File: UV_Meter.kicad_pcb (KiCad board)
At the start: 2 copper layers, 58.4 x 17.8 mm, 8 parts, among them SW1 SW_Push, U1 ATtiny85-20PU

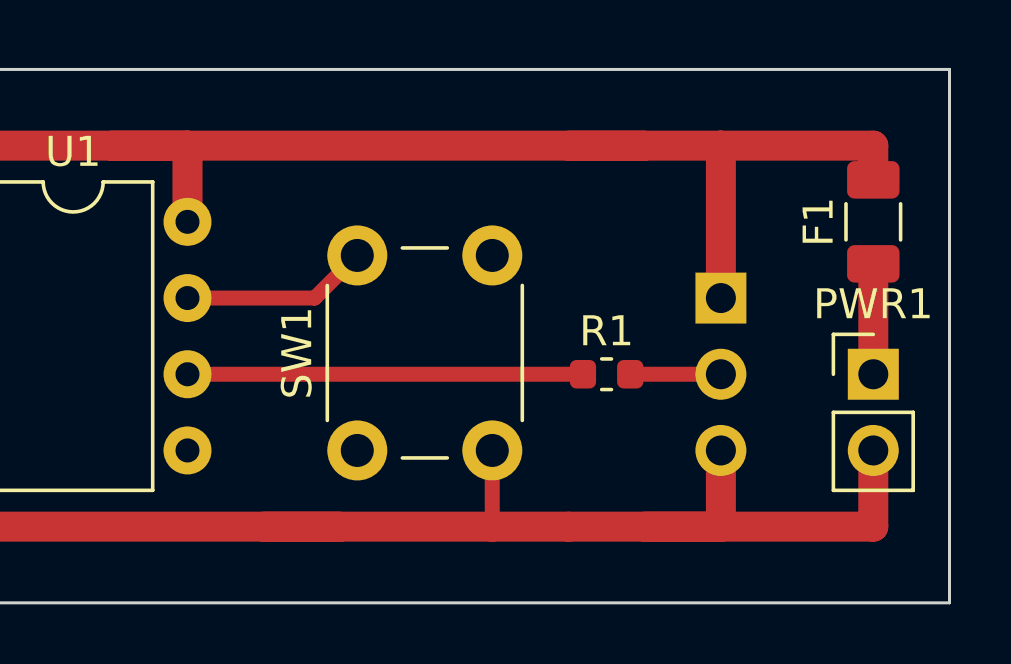
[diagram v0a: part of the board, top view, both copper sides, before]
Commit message: switched PWR & LED
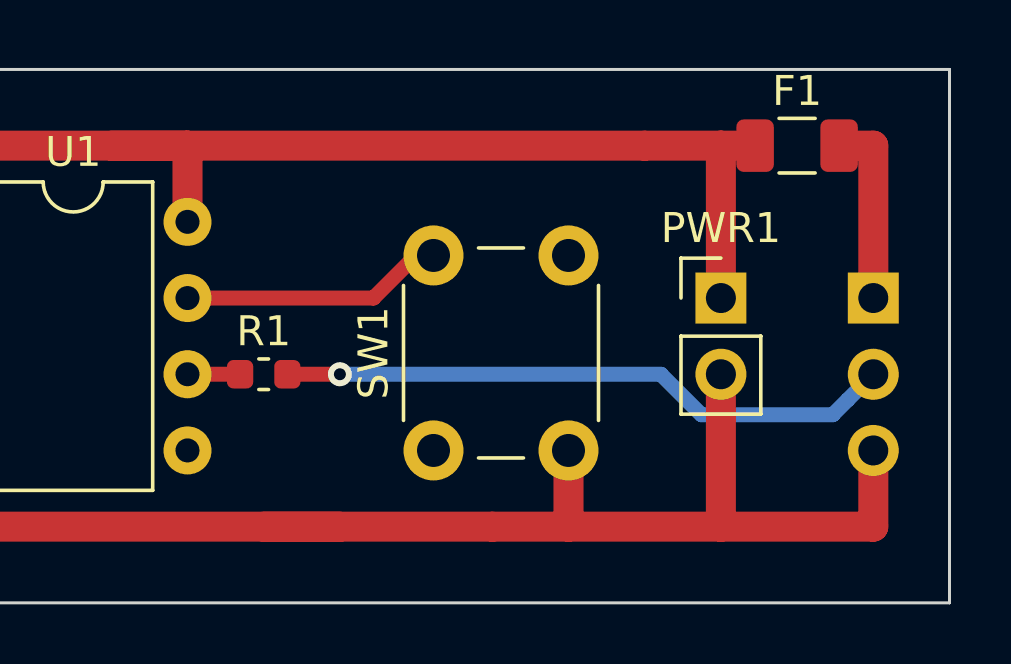
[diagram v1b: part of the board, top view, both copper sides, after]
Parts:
- moved R1 11.4 mm to (58.4, 30.5)
- moved PWR1 5.68 mm to (73.7, 27.9)
- moved RGB1 5.08 mm to (78.7, 27.9)
- moved F1 3.59 mm to (76.2, 22.9), turned to 0 degrees
- moved SW1 2.54 mm to (64.1, 33.0)
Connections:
- F1 pad 2: +5V -> /F_5V
- R1 pad 2: /data -> /R_data
- RGB1 pad 1: +5V -> /F_5V
- RGB1 pad 2: /data -> /R_data
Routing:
- net /R_data: track 0.00 -> 20.7 mm, vias 0 -> 1
- net /data: track 16.2 -> 1.75 mm
- net +5V: track 81.0 -> 69.7 mm
- net /F_5V: track 0.00 -> 6.22 mm
- net /bt_inv: track 6.25 -> 8.21 mm
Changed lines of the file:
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@@
     (thickness 1.6)
     (drawings 9)
-    (tracks 35)
+    (tracks 40)
     (zones 0)
     (modules 8)
-    (nets 6)
+    (nets 8)
   )
   (page A4)
@@
   )
   (setup
-    (last_trace_width 0.25)
+    (last_trace_width 1)
     (user_trace_width 0.25)
     (user_trace_width 0.5)
@@
   (net 4 /bt_inv)
   (net 5 /AO)
+  (net 6 /F_5V)
+  (net 7 /R_data)
   (net_class Default "This is the default net class."
     (clearance 0.25)
@@
     (add_net +5V)
     (add_net /AO)
+    (add_net /F_5V)
+    (add_net /R_data)
     (add_net /bt_inv)
     (add_net /data)
@@
   )
   (module Connector_PinHeader_2.54mm:PinHeader_1x03_P2.54mm_Vertical (layer B.Cu)
-    (at 73.66 27.94 180)
+    (at 78.74 27.94 180)
     (descr "Through hole straight pin header, 1x03, 2.54mm pitch, single row")
     (tags "Through hole pin header THT 1x03 2.54mm single row")
@@
       (net 1 GND))
     (pad 2 thru_hole oval (at 0 -2.54 180) (size 1.7 1.7) (drill 1) (layers *.Cu *.Mask)
-      (net 3 /data))
+      (net 7 /R_data))
     (pad 1 thru_hole rect (at 0 0 180) (size 1.7 1.7) (drill 1) (layers *.Cu *.Mask)
-      (net 2 +5V))
+      (net 6 /F_5V))
     (model ${KISYS3DMOD}/Connector_PinHeader_2.54mm.3dshapes/PinHeader_1x03_P2.54mm_Vertical.wrl
       (at (xyz 0 0 0))
@@
   )
   (module Connector_PinHeader_2.54mm:PinHeader_1x02_P2.54mm_Vertical (layer F.Cu)
-    (at 78.74 30.48)
+    (at 73.66 27.94)
     (descr "Through hole straight pin header, 1x02, 2.54mm pitch, single row")
     (tags "Through hole pin header THT 1x02 2.54mm single row")
@@
   )
   (module Fuse:Fuse_1206_3216Metric (layer F.Cu)
-    (at 78.74 25.4 90)
+    (at 76.2 22.86)
     (descr "Fuse SMD 1206 (3216 Metric), square (rectangular) end terminal, IPC_7351 nominal, (Body size source: http://www.tortai-tech.com/upload/download/2011102023233369053.pdf), generated with kicad-footprint-generator")
     (tags resistor)
     (attr smd)
-    (fp_text reference F1 (at 0 -1.82 90) (layer F.SilkS)
-      (effects (font (size 1 1) (thickness 0.15)))
-    )
-    (fp_text value Polyfuse (at 0 1.82 90) (layer F.Fab)
-      (effects (font (size 1 1) (thickness 0.15)))
-    )
-    (fp_text user %R (at 0 0 90) (layer F.Fab)
+    (fp_text reference F1 (at 0 -1.82) (layer F.SilkS)
+      (effects (font (size 1 1) (thickness 0.15)))
+    )
+    (fp_text value Polyfuse (at 0 1.82) (layer F.Fab)
+      (effects (font (size 1 1) (thickness 0.15)))
+    )
+    (fp_text user %R (at 0 0) (layer F.Fab)
       (effects (font (size 0.8 0.8) (thickness 0.12)))
     )
@@
     (fp_line (start -1.6 -0.8) (end 1.6 -0.8) (layer F.Fab) (width 0.1))
     (fp_line (start -1.6 0.8) (end -1.6 -0.8) (layer F.Fab) (width 0.1))
-    (pad 2 smd roundrect (at 1.4 0 90) (size 1.25 1.75) (layers F.Cu F.Paste F.Mask) (roundrect_rratio 0.2)
-      (net 2 +5V))
-    (pad 1 smd roundrect (at -1.4 0 90) (size 1.25 1.75) (layers F.Cu F.Paste F.Mask) (roundrect_rratio 0.2)
+    (pad 2 smd roundrect (at 1.4 0) (size 1.25 1.75) (layers F.Cu F.Paste F.Mask) (roundrect_rratio 0.2)
+      (net 6 /F_5V))
+    (pad 1 smd roundrect (at -1.4 0) (size 1.25 1.75) (layers F.Cu F.Paste F.Mask) (roundrect_rratio 0.2)
       (net 2 +5V))
     (model ${KISYS3DMOD}/Fuse.3dshapes/Fuse_1206_3216Metric.wrl
@@
   )
   (module Button_Switch_THT:SW_PUSH_6mm_H4.3mm (layer F.Cu)
-    (at 61.54 33.02 90)
+    (at 64.08 33.02 90)
     (descr "tactile push button, 6x6mm e.g. PHAP33xx series, height=4.3mm")
     (tags "tact sw push 6mm")
@@
   )
   (module Resistor_SMD:R_0603_1608Metric (layer F.Cu)
-    (at 69.85 30.48)
+    (at 58.42 30.48)
     (descr "Resistor SMD 0603 (1608 Metric), square (rectangular) end terminal, IPC_7351 nominal, (Body size source: http://www.tortai-tech.com/upload/download/2011102023233369053.pdf), generated with kicad-footprint-generator")
     (tags resistor)
@@
     (fp_line (start -0.8 0.4) (end -0.8 -0.4) (layer F.Fab) (width 0.1))
     (pad 2 smd roundrect (at 0.7875 0) (size 0.875 0.95) (layers F.Cu F.Paste F.Mask) (roundrect_rratio 0.25)
-      (net 3 /data))
+      (net 7 /R_data))
     (pad 1 smd roundrect (at -0.7875 0) (size 0.875 0.95) (layers F.Cu F.Paste F.Mask) (roundrect_rratio 0.25)
       (net 3 /data))
@@
   (gr_line (start 81.28 20.32) (end 81.28 38.1) (layer Edge.Cuts) (width 0.1))
   (segment (start 60.96 35.56) (end 48.26 35.56) (width 1) (layer F.Cu) (net 1))
-  (segment (start 73.66 33.02) (end 73.66 35.56) (width 1) (layer F.Cu) (net 1))
-  (segment (start 73.66 35.56) (end 71.12 35.56) (width 1) (layer F.Cu) (net 1))
+  (segment (start 78.74 33.02) (end 78.74 35.56) (width 1) (layer F.Cu) (net 1))
   (segment (start 48.26 35.56) (end 43.18 35.56) (width 1) (layer F.Cu) (net 1))
   (segment (start 34.222081 35.56) (end 43.18 35.56) (width 1) (layer F.Cu) (net 1))
-  (segment (start 78.74 35.56) (end 78.74 33.02) (width 1) (layer F.Cu) (net 1))
-  (segment (start 73.66 35.56) (end 78.74 35.56) (width 1) (layer F.Cu) (net 1))
   (segment (start 25.4 30.48) (end 27.94 30.48) (width 1) (layer F.Cu) (net 1))
   (segment (start 27.94 35.56) (end 34.222081 35.56) (width 1) (layer F.Cu) (net 1))
@@
   (segment (start 43.18 35.56) (end 43.18 30.44) (width 1) (layer F.Cu) (net 1))
   (segment (start 48.26 35.56) (end 48.26 33.02) (width 1) (layer F.Cu) (net 1))
-  (segment (start 68.58 35.56) (end 66.04 35.56) (width 1) (layer F.Cu) (net 1))
-  (segment (start 73.66 35.56) (end 68.58 35.56) (width 1) (layer F.Cu) (net 1))
-  (segment (start 66.04 33.02) (end 66.04 35.56) (width 0.5) (layer F.Cu) (net 1))
+  (segment (start 73.66 30.48) (end 73.66 35.56) (width 1) (layer F.Cu) (net 1))
+  (segment (start 73.66 35.56) (end 78.74 35.56) (width 1) (layer F.Cu) (net 1))
+  (segment (start 68.58 33.02) (end 68.58 35.56) (width 1) (layer F.Cu) (net 1))
+  (segment (start 66.04 35.56) (end 68.58 35.56) (width 1) (layer F.Cu) (net 1))
+  (segment (start 68.58 35.56) (end 73.66 35.56) (width 1) (layer F.Cu) (net 1))
   (segment (start 43.18 27.94) (end 43.18 22.86) (width 1) (layer F.Cu) (net 2))
   (segment (start 55.88 25.4) (end 55.88 22.86) (width 1) (layer F.Cu) (net 2))
-  (segment (start 78.74 26.8) (end 78.74 30.48) (width 1) (layer F.Cu) (net 2))
   (segment (start 71.12 22.86) (end 53.34 22.86) (width 1) (layer F.Cu) (net 2))
-  (segment (start 73.66 27.94) (end 73.66 22.86) (width 1) (layer F.Cu) (net 2))
-  (segment (start 73.66 22.86) (end 68.58 22.86) (width 1) (layer F.Cu) (net 2))
   (segment (start 55.88 22.86) (end 43.18 22.86) (width 1) (layer F.Cu) (net 2))
   (segment (start 43.18 22.86) (end 30.48 22.86) (width 1) (layer F.Cu) (net 2))
-  (segment (start 78.74 22.86) (end 78.74 24) (width 1) (layer F.Cu) (net 2))
-  (segment (start 73.66 22.86) (end 78.74 22.86) (width 1) (layer F.Cu) (net 2))
   (segment (start 25.4 27.94) (end 27.94 27.94) (width 1) (layer F.Cu) (net 2))
   (segment (start 27.94 27.94) (end 27.94 22.86) (width 1) (layer F.Cu) (net 2))
   (segment (start 27.94 22.86) (end 30.48 22.86) (width 1) (layer F.Cu) (net 2))
-  (segment (start 70.6375 30.48) (end 73.66 30.48) (width 0.5) (layer F.Cu) (net 3))
-  (segment (start 69.0625 30.48) (end 55.88 30.48) (width 0.5) (layer F.Cu) (net 3))
-  (segment (start 55.88 27.94) (end 60.12 27.94) (width 0.5) (layer F.Cu) (net 4))
-  (segment (start 60.12 27.94) (end 61.54 26.52) (width 0.5) (layer F.Cu) (net 4))
+  (segment (start 73.66 27.94) (end 73.66 22.86) (width 1) (layer F.Cu) (net 2))
+  (segment (start 71.12 22.86) (end 73.66 22.86) (width 1) (layer F.Cu) (net 2))
+  (segment (start 73.66 22.86) (end 74.8 22.86) (width 1) (layer F.Cu) (net 2))
+  (segment (start 55.88 30.48) (end 57.6325 30.48) (width 0.5) (layer F.Cu) (net 3))
+  (segment (start 62.08 27.94) (end 63.5 26.52) (width 0.5) (layer F.Cu) (net 4))
+  (segment (start 55.88 27.94) (end 62.08 27.94) (width 0.5) (layer F.Cu) (net 4))
+  (segment (start 77.6 22.86) (end 78.74 22.86) (width 1) (layer F.Cu) (net 6))
+  (segment (start 78.74 22.86) (end 78.74 27.94) (width 1) (layer F.Cu) (net 6))
   (segment (start 45.72 33.02) (end 48.26 30.48) (width 0.5) (layer B.Cu) (net 5))
   (segment (start 25.4 33.02) (end 45.72 33.02) (width 0.5) (layer B.Cu) (net 5))
+  (via (at 60.96 30.48) (size 0.8) (drill 0.4) (layers F.Cu B.Cu) (net 7))
+  (segment (start 59.2075 30.48) (end 60.96 30.48) (width 0.5) (layer F.Cu) (net 7))
+  (segment (start 77.890001 31.329999) (end 78.74 30.48) (width 0.5) (layer B.Cu) (net 7))
+  (segment (start 77.389999 31.830001) (end 77.890001 31.329999) (width 0.5) (layer B.Cu) (net 7))
+  (segment (start 73.011999 31.830001) (end 77.389999 31.830001) (width 0.5) (layer B.Cu) (net 7))
+  (segment (start 71.661998 30.48) (end 73.011999 31.830001) (width 0.5) (layer B.Cu) (net 7))
+  (segment (start 60.96 30.48) (end 71.661998 30.48) (width 0.5) (layer B.Cu) (net 7))
   (zone (net 0) (net_name "") (layer F.Cu) (hatch edge 0.508)
     (connect_pads (clearance 0.508))

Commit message: added mounting holes and played around
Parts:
- added H1: MountingHole, MountingHole:MountingHole_3.2mm_M3_ISO14580, F.Cu at (35.6, 29.2)
- added R_reset1: 10k, Resistor_SMD:R_0603_1608Metric, F.Cu at (45.7, 25.4)
- F_LED1: renamed from F1; value Polyfuse -> 500mA
- moved R_data1 10.2 mm to (68.6, 30.5)
- moved SW1 3.12 mm to (61.0, 33.0)
- renumbered R1 to R_data1
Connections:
- net /F_5V renamed /fused_5V
- net /R_data renamed /r_data
- U1 pad 1: (no net) -> /reset
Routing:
- net /data: track 1.75 -> 11.9 mm
- net /r_data: track 20.7 -> 10.5 mm
- net /bt_inv: track 8.21 -> 5.67 mm
- net /reset: track 0.00 -> 1.75 mm
- net +5V: track 69.7 -> 71.5 mm

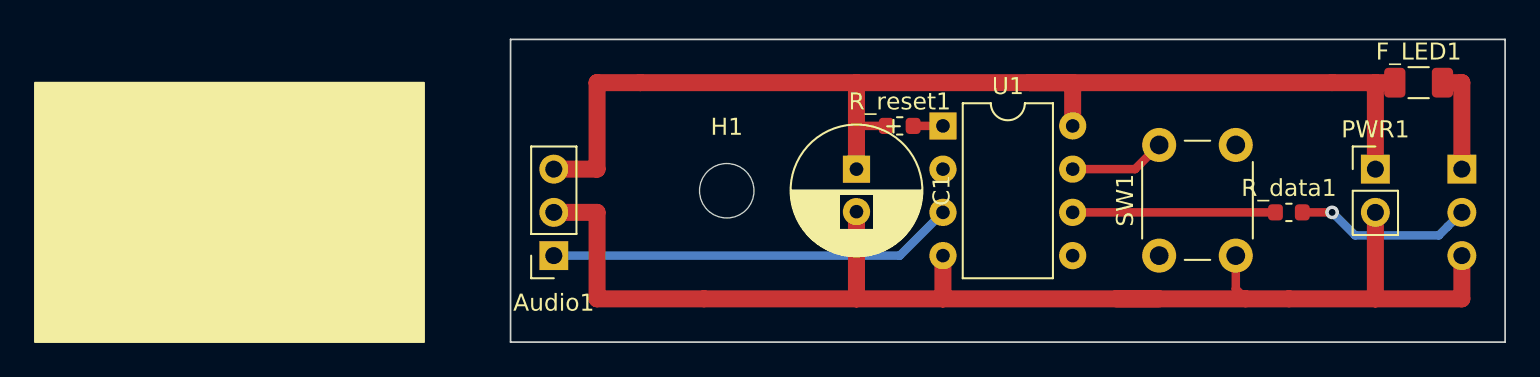
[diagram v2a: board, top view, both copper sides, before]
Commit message: use official kicad gitignore, (re)move Gerber
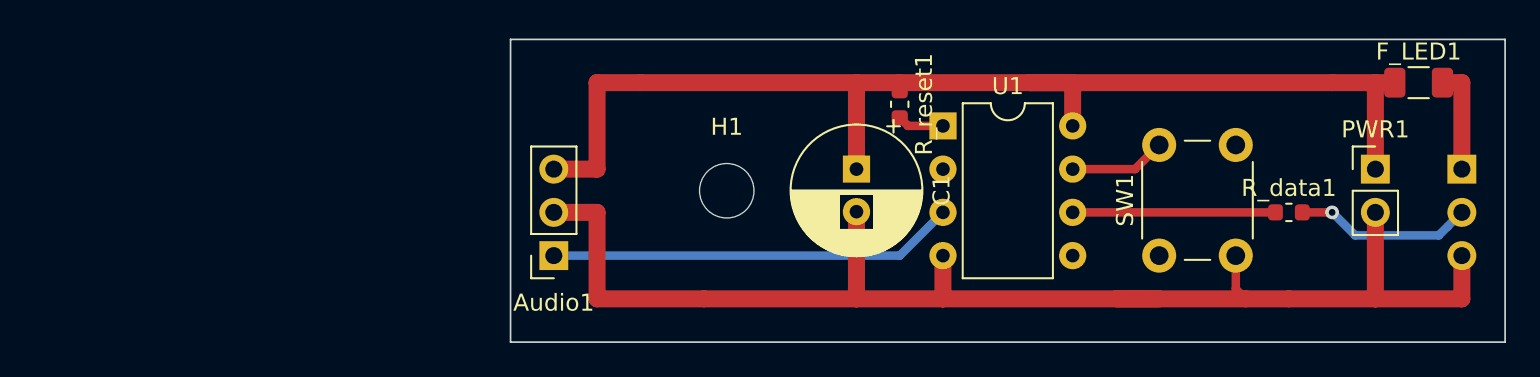
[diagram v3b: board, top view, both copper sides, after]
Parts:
- moved R_reset1 1.27 mm to (45.7, 24.1), turned to 270 degrees
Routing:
- net +5V: track 71.5 -> 70.2 mm
- net /reset: track 1.75 -> 2.74 mm
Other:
- rule via_min_size: 0.4 -> 0.6
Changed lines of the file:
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@@
   (general
     (thickness 1.6)
-    (drawings 9)
-    (tracks 43)
+    (drawings 6)
+    (tracks 45)
     (zones 0)
     (modules 10)
@@
     (via_size 0.8)
     (via_drill 0.4)
-    (via_min_size 0.4)
+    (via_min_size 0.6)
     (via_min_drill 0.3)
     (uvia_size 0.3)
@@
       (drillshape 0)
       (scaleselection 1)
-      (outputdirectory "./"))
+      (outputdirectory "Gerber/"))
   )
   (net 0 "")
@@
   )
   (module Resistor_SMD:R_0603_1608Metric (layer F.Cu)
-    (at 45.72 25.4)
+    (at 45.72 24.13 270)
     (descr "Resistor SMD 0603 (1608 Metric), square (rectangular) end terminal, IPC_7351 nominal, (Body size source: http://www.tortai-tech.com/upload/download/2011102023233369053.pdf), generated with kicad-footprint-generator")
     (tags resistor)
     (attr smd)
-    (fp_text reference R_reset1 (at 0 -1.43) (layer F.SilkS)
-      (effects (font (size 1 1) (thickness 0.15)))
-    )
-    (fp_text value 10k (at 0 1.43) (layer F.Fab)
-      (effects (font (size 1 1) (thickness 0.15)))
-    )
-    (fp_text user %R (at 0 0) (layer F.Fab)
+    (fp_text reference R_reset1 (at 0 -1.43 270) (layer F.SilkS)
+      (effects (font (size 1 1) (thickness 0.15)))
+    )
+    (fp_text value 10k (at 0 1.43 270) (layer F.Fab)
+      (effects (font (size 1 1) (thickness 0.15)))
+    )
+    (fp_text user %R (at 0 0 270) (layer F.Fab)
       (effects (font (size 0.4 0.4) (thickness 0.06)))
     )
@@
     (fp_line (start -0.8 -0.4) (end 0.8 -0.4) (layer F.Fab) (width 0.1))
     (fp_line (start -0.8 0.4) (end -0.8 -0.4) (layer F.Fab) (width 0.1))
-    (pad 2 smd roundrect (at 0.7875 0) (size 0.875 0.95) (layers F.Cu F.Paste F.Mask) (roundrect_rratio 0.25)
+    (pad 2 smd roundrect (at 0.7875 0 270) (size 0.875 0.95) (layers F.Cu F.Paste F.Mask) (roundrect_rratio 0.25)
       (net 8 /reset))
-    (pad 1 smd roundrect (at -0.7875 0) (size 0.875 0.95) (layers F.Cu F.Paste F.Mask) (roundrect_rratio 0.25)
+    (pad 1 smd roundrect (at -0.7875 0 270) (size 0.875 0.95) (layers F.Cu F.Paste F.Mask) (roundrect_rratio 0.25)
       (net 2 +5V))
     (model ${KISYS3DMOD}/Resistor_SMD.3dshapes/R_0603_1608Metric.wrl
@@
       (effects (font (size 1 1) (thickness 0.15)))
     )
-    (fp_text value Conn_01x03 (at 0 7.85 180) (layer F.Fab)
+    (fp_text value Conn_01x03 (at 0 7.85 180) (layer F.Fab) hide
       (effects (font (size 1 1) (thickness 0.15)))
     )
@@
       (effects (font (size 1 1) (thickness 0.15)) (justify mirror))
     )
-    (fp_text value Conn_01x03 (at 0 -7.41 180) (layer B.Fab)
+    (fp_text value Conn_01x03 (at 0 -7.41 180) (layer B.Fab) hide
       (effects (font (size 1 1) (thickness 0.15)) (justify mirror))
     )
@@
     )
   )
-  (dimension 15.24 (width 0.12) (layer F.SilkS)
-    (gr_text "15.240 mm" (at -11.43 30.48 270) (layer F.SilkS)
-      (effects (font (size 1 1) (thickness 0.15)))
-    )
-    (feature1 (pts (xy -5.080001 38.1) (xy -10.746421 38.1)))
-    (feature2 (pts (xy -5.080001 22.86) (xy -10.746421 22.86)))
-    (crossbar (pts (xy -10.16 22.86) (xy -10.16 38.1)))
-    (arrow1a (pts (xy -10.16 38.1) (xy -10.746421 36.973496)))
-    (arrow1b (pts (xy -10.16 38.1) (xy -9.573579 36.973496)))
-    (arrow2a (pts (xy -10.16 22.86) (xy -10.746421 23.986504)))
-    (arrow2b (pts (xy -10.16 22.86) (xy -9.573579 23.986504)))
-  )
-  (dimension 17.78 (width 0.12) (layer F.SilkS)
-    (gr_text "17.780 mm" (at 87.63 29.21 270) (layer F.SilkS)
+  (dimension 17.78 (width 0.12) (layer Dwgs.User)
+    (gr_text "17.780 mm" (at 87.63 29.21 270) (layer Dwgs.User)
       (effects (font (size 1 1) (thickness 0.15)))
     )
@@
     (arrow2b (pts (xy 86.36 20.32) (xy 86.946421 21.446504)))
   )
-  (dimension 58.42 (width 0.12) (layer F.SilkS)
-    (gr_text "58.420 mm" (at 52.07 44.45) (layer F.SilkS)
+  (dimension 58.42 (width 0.12) (layer Dwgs.User)
+    (gr_text "58.420 mm" (at 52.07 44.45) (layer Dwgs.User)
       (effects (font (size 1 1) (thickness 0.15)))
     )
@@
     (arrow2b (pts (xy 81.28 43.18) (xy 80.153496 43.766421)))
   )
-  (dimension 22.86 (width 0.12) (layer F.SilkS)
-    (gr_text "22.860 mm" (at 6.35 44.45) (layer F.SilkS)
-      (effects (font (size 1 1) (thickness 0.15)))
-    )
-    (feature1 (pts (xy -5.08 38.1) (xy -5.08 43.766421)))
-    (feature2 (pts (xy 17.78 38.1) (xy 17.78 43.766421)))
-    (crossbar (pts (xy 17.78 43.18) (xy -5.08 43.18)))
-    (arrow1a (pts (xy -5.08 43.18) (xy -3.953496 42.593579)))
-    (arrow1b (pts (xy -5.08 43.18) (xy -3.953496 43.766421)))
-    (arrow2a (pts (xy 17.78 43.18) (xy 16.653496 42.593579)))
-    (arrow2b (pts (xy 17.78 43.18) (xy 16.653496 43.766421)))
-  )
-  (gr_poly (pts (xy -5.08 22.86) (xy 17.78 22.86) (xy 17.78 38.1) (xy -5.08 38.1)) (layer F.SilkS) (width 0.1))
   (gr_line (start 22.86 20.32) (end 81.28 20.32) (layer Edge.Cuts) (width 0.1))
   (gr_line (start 22.86 38.1) (end 22.86 20.32) (layer Edge.Cuts) (width 0.1))
@@
   (segment (start 55.88 25.4) (end 55.88 22.86) (width 1) (layer F.Cu) (net 2))
   (segment (start 71.12 22.86) (end 53.34 22.86) (width 1) (layer F.Cu) (net 2))
-  (segment (start 55.88 22.86) (end 43.18 22.86) (width 1) (layer F.Cu) (net 2))
   (segment (start 43.18 22.86) (end 30.48 22.86) (width 1) (layer F.Cu) (net 2))
   (segment (start 25.4 27.94) (end 27.94 27.94) (width 1) (layer F.Cu) (net 2))
@@
   (segment (start 71.12 22.86) (end 73.66 22.86) (width 1) (layer F.Cu) (net 2))
   (segment (start 73.66 22.86) (end 74.8 22.86) (width 1) (layer F.Cu) (net 2))
-  (segment (start 44.9325 25.4) (end 43.18 25.4) (width 0.5) (layer F.Cu) (net 2))
   (segment (start 43.18 27.94) (end 43.18 25.4) (width 1) (layer F.Cu) (net 2))
   (segment (start 43.18 25.4) (end 43.18 22.86) (width 1) (layer F.Cu) (net 2))
+  (segment (start 45.72 23.3425) (end 45.72 22.86) (width 0.5) (layer F.Cu) (net 2))
+  (segment (start 55.88 22.86) (end 45.72 22.86) (width 1) (layer F.Cu) (net 2))
+  (segment (start 45.72 22.86) (end 43.18 22.86) (width 1) (layer F.Cu) (net 2))
   (segment (start 55.88 30.48) (end 67.7925 30.48) (width 0.5) (layer F.Cu) (net 3))
   (segment (start 59.54 27.94) (end 60.96 26.52) (width 0.5) (layer F.Cu) (net 4))
@@
   (segment (start 72.470001 31.830001) (end 77.389999 31.830001) (width 0.5) (layer B.Cu) (net 7))
   (segment (start 71.12 30.48) (end 72.470001 31.830001) (width 0.5) (layer B.Cu) (net 7))
-  (segment (start 48.26 25.4) (end 46.5075 25.4) (width 0.5) (layer F.Cu) (net 8))
+  (segment (start 46.2025 25.4) (end 45.72 24.9175) (width 0.5) (layer F.Cu) (net 8))
+  (segment (start 48.26 25.4) (end 46.2025 25.4) (width 0.5) (layer F.Cu) (net 8))
   (zone (net 0) (net_name "") (layer F.Cu) (hatch edge 0.508)
     (connect_pads (clearance 0.508))
